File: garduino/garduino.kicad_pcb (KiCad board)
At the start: 2 copper layers, 65 x 56 mm, 54 parts, among them J1 ADC1, J10 OUT6, J11 ADC7, J12 OUT5, J13 OUT4, J14 DIN, J15 OUT3, J16 12v, J17 OUT2, J18 OUT1, J19 RPi, J2 ADC2, J3 ADC3, J4 Max7219, J5 ADC4, J6 ADC5, J7 OUT8, J8 OUT7, J9 ADC6, Q1 NCV8403, Q10 BSS138, Q11 BSS138, Q12 NCV8403, Q2 NCV8403, Q3 NCV8403, Q4 NCV8403, Q5 NCV8403, Q6 NCV8403, Q7 NCV8403, Q8 BSS138, Q9 BSS138, SW1 SW_DIP_x01, U2 ATmega328P-AU, Y1 Crystal

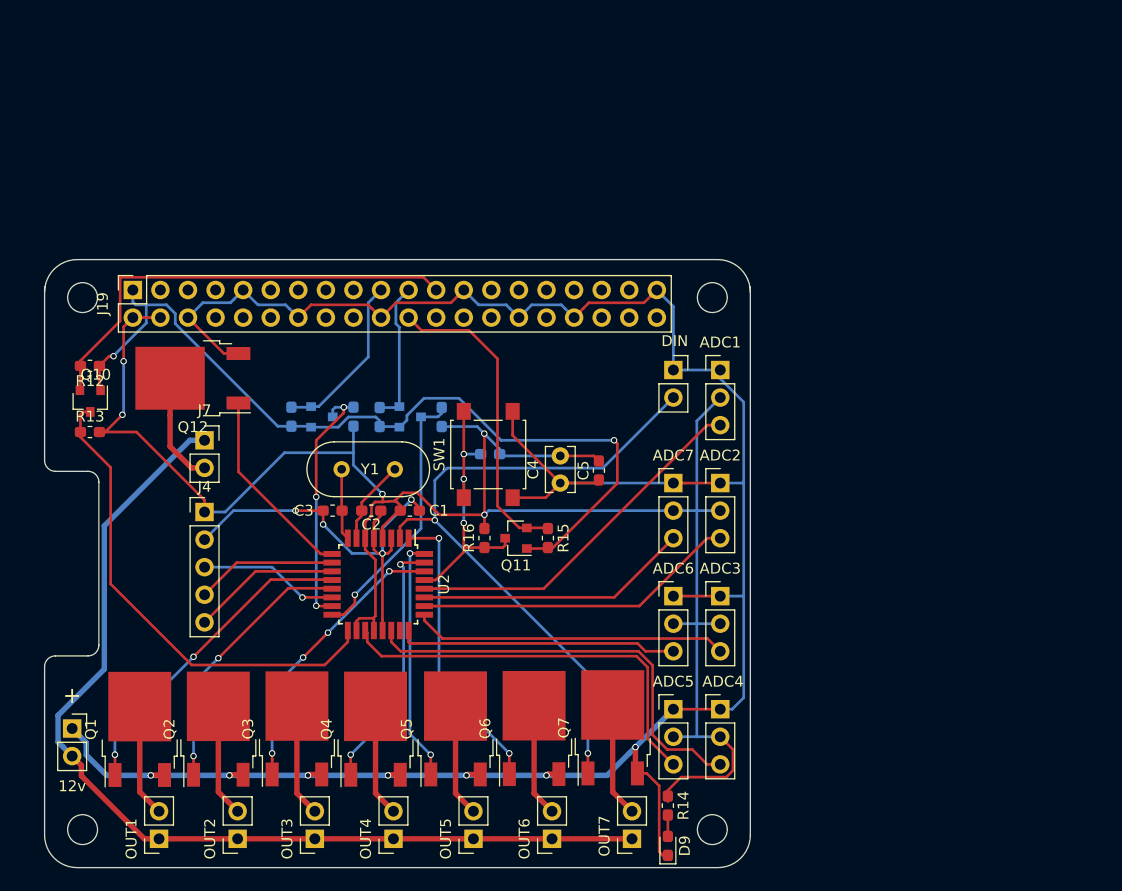
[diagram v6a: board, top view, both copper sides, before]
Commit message: Guarduino switched to MCP3008, PCB not done
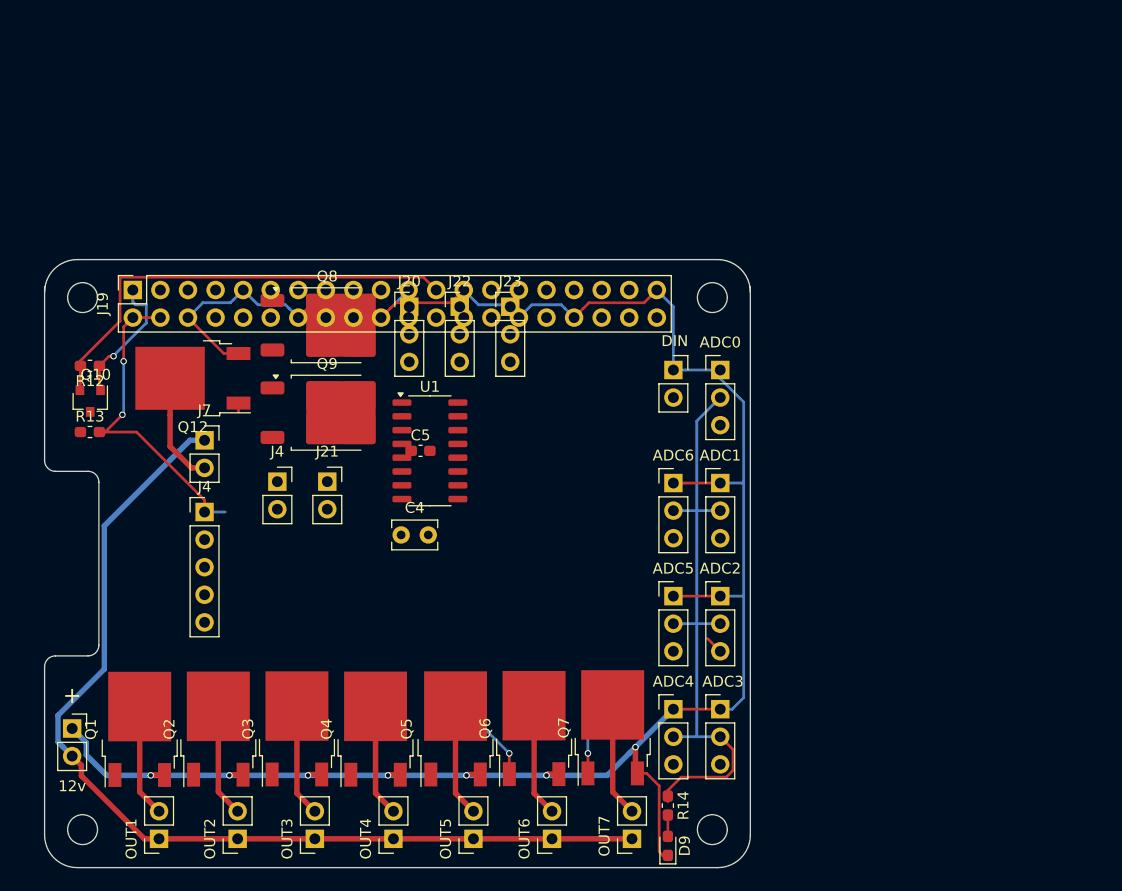
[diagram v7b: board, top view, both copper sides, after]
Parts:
- removed C1: 100n, Capacitor_SMD:C_0603_1608Metric_Pad1.05x0.95mm_HandSolder
- removed C2, C3: 22pF, Capacitor_SMD:C_0603_1608Metric_Pad1.05x0.95mm_HandSolder
- removed Q11: BSS138, Package_TO_SOT_SMD:SOT-23
- removed R10, R11, R15, R16, R17, R8, R9: 10k, Resistor_SMD:R_0603_1608Metric_Pad1.05x0.95mm_HandSolder
- removed SW1: SW_DIP_x01, Button_Switch_SMD:SW_SPST_B3S-1000
- removed U2: ATmega328P-AU, Package_QFP:TQFP-32_7x7mm_P0.8mm
- removed Y1: Crystal, Crystal:Crystal_HC18-U_Vertical
- added J20: ADC7, Connector_PinHeader_2.54mm:PinHeader_1x03_P2.54mm_Vertical, F.Cu at (123.2, 93.0)
- added J21: OUT1, Connector_PinSocket_2.54mm:PinSocket_1x02_P2.54mm_Vertical, F.Cu at (115.7, 109.1)
- added J22: ADC8, Connector_PinHeader_2.54mm:PinHeader_1x03_P2.54mm_Vertical, F.Cu at (127.9, 93.0)
- added J23: ADC9, Connector_PinHeader_2.54mm:PinHeader_1x03_P2.54mm_Vertical, F.Cu at (132.6, 93.0)
- added J4: OUT1, Connector_PinSocket_2.54mm:PinSocket_1x02_P2.54mm_Vertical, F.Cu at (111.1, 109.1)
- added U1: MCP3008, Package_SO:SO-16_3.9x9.9mm_P1.27mm, F.Cu at (125.2, 106.2)
- C5: footprint Capacitor_SMD:C_0603_1608Metric_Pad1.05x0.95mm_HandSolder -> Capacitor_SMD:C_0603_1608Metric_Pad1.08x0.95mm_HandSolder
- J1: value ADC1 -> ADC0
- J11: value ADC7 -> ADC6
- J2: value ADC2 -> ADC1
- J3: value ADC3 -> ADC2
- J5: value ADC4 -> ADC3
- J6: value ADC5 -> ADC4
- J9: value ADC6 -> ADC5
- Q8, Q9: value BSS138 -> NCV8403; footprint Package_TO_SOT_SMD:SOT-23 -> Package_TO_SOT_SMD:TO-252-2; moved to F.Cu
- moved C5 16.5 mm to (124.3, 106.2), turned to 0 degrees
- moved C4 15.4 mm to (122.5, 114.0), turned to 0 degrees
- moved Q8 8.45 mm to (115.7, 94.7)
- moved Q9 7.65 mm to (115.7, 102.7)
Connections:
- J1 pad 3: /PC5 -> /CH0
- J11 pad 3: /PC4 -> /CH6
- J19 pad 1: +3V3 -> +3.3V
- J19 pad 10: (no net) -> /RXD
- J19 pad 11: (no net) -> /SPI1_CE1
- J19 pad 12: (no net) -> /SPI1_CE0
- J19 pad 13: (no net) -> /GPIO27
- J19 pad 15: (no net) -> /GPIO22
- J19 pad 16: (no net) -> /GPIO23
- J19 pad 17: (no net) -> +3.3V
- J19 pad 18: (no net) -> /GPIO24
- J19 pad 22: /BCM25 -> /GPIO25
- J19 pad 24: (no net) -> /SPI0_CE0
- J19 pad 26: (no net) -> /SPI0_CE1
- J19 pad 27: (no net) -> /GPIO0
- J19 pad 28: (no net) -> /GPIO1
- J19 pad 29: (no net) -> /GPIO5
- J19 pad 3: (no net) -> /SDA
- J19 pad 31: (no net) -> /GPIO6
- J19 pad 32: (no net) -> /PWM0
- J19 pad 33: (no net) -> /PWM1
- J19 pad 35: (no net) -> /SPI1_MISO
- J19 pad 36: (no net) -> /SPI1_CE2
- J19 pad 37: (no net) -> /GPIO26
- J19 pad 38: (no net) -> /SPI1_MOSI
- J19 pad 40: (no net) -> /SPI1_SCLK
- J19 pad 5: (no net) -> /SCL
- J19 pad 7: (no net) -> /GPIO4
- J19 pad 8: (no net) -> /TXD
- J2 pad 3: /PC3 -> /CH1
- J3 pad 3: /PC2 -> /CH2
- J5 pad 3: /ADC7 -> /CH3
- J6 pad 3: /ADC6 -> /CH4
- J9 pad 3: /PC1 -> /CH5
- Q1 pad 1: /PB0 -> /GPIO4
- Q10 pad 1: +3V3 -> +3.3V
- Q12 pad 1: /PD5 -> /GPIO24
- Q2 pad 1: /PB1 -> /GPIO27
- Q3 pad 1: /PD0 -> /GPIO22
- Q4 pad 1: /PD1 -> /GPIO0
- Q5 pad 1: /PD2 -> /GPIO5
- Q6 pad 1: /PD3 -> /GPIO6
- Q7 pad 1: /PD4 -> /GPIO23
- Q8 pad 1: +3V3 -> /GPIO25
- Q8 pad 2: /SPI0_MOSI -> /OUT8
- Q8 pad 3: /MOSI -> GND
- Q9 pad 1: +3V3 -> /GPIO1
- Q9 pad 2: /SPI0_MISO -> /OUT9
- Q9 pad 3: /MISO -> GND
- R12 pad 2: +3V3 -> +3.3V
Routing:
- net +5V: track 182.0 -> 86.6 mm, vias 5 -> 2
- net +3V3: track 79.7 -> 0.00 mm, vias 2 -> 0
- net GND: track 269.3 -> 200.7 mm, vias 11 -> 7
- net /PD4: track 62.5 -> 0.00 mm, vias 2 -> 0
- net /SCLK: track 44.6 -> 0.00 mm
- net /ADC7: track 39.8 -> 0.00 mm
- net /ADC6: track 37.8 -> 0.00 mm
- net /PC5: track 33.5 -> 0.00 mm
- net /PC3: track 29.8 -> 0.00 mm
- net /PB0: track 29.6 -> 0.00 mm, vias 2 -> 0
- net /PC2: track 29.0 -> 0.00 mm
- net /BCM25: track 28.8 -> 0.00 mm
- net /PD3: track 27.2 -> 0.00 mm, vias 2 -> 0
- net /PD0: track 26.6 -> 0.00 mm, vias 4 -> 0
- net /PC1: track 25.8 -> 0.00 mm
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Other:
- net class Default removed

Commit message: Cleanups, placement might work
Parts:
- removed the J14 at (147.6, 98.8)
- removed the J4 at (104.4, 111.9)
- removed the Q10 at (93.9, 101.7)
- removed R12, R13: 10k, Resistor_SMD:R_0603_1608Metric_Pad1.05x0.95mm_HandSolder
- J10: renamed from J8; value OUT7 -> OUT6
- J11: renamed from J7; value OUT8 -> OUT7
- J12: renamed from J21; value OUT1 -> OUT8
- J13: renamed from J4; value OUT1 -> OUT9
- J4: renamed from J18; value OUT1 -> OUT0
- J5: renamed from J17; value OUT2 -> OUT1
- J6: renamed from J15; value OUT3 -> OUT2
- J7: renamed from J13; value OUT4 -> OUT3
- J8: renamed from J12; value OUT5 -> OUT4
- J9: renamed from J10; value OUT6 -> OUT5
- moved R1 56.3 mm to (96.0, 115.2)
- moved D1 56.3 mm to (96.0, 118.9)
- moved J11 47.5 mm to (134.5, 142.0), turned to 180 degrees
- moved J13 46.9 mm to (144.5, 142.0), turned to 180 degrees
- moved J23 46.1 mm to (151.5, 135.0), turned to -90 degrees
- moved J22 44.4 mm to (151.6, 130.5), turned to -90 degrees
- moved J21 43.5 mm to (151.5, 126.0), turned to -90 degrees
- moved J12 40.6 mm to (139.5, 142.0), turned to 180 degrees
- moved Q4 31.3 mm to (113.0, 120.0)
- moved Q8 27.4 mm to (128.0, 119.2), turned to 90 degrees
- moved Q5 26.7 mm to (120.5, 120.0), turned to 90 degrees
- moved Q10 26.0 mm to (135.8, 119.2), turned to 90 degrees
- moved J17 20.1 mm to (151.5, 110.0), turned to -90 degrees
- moved J18 16.5 mm to (151.5, 114.0), turned to -90 degrees
- moved J10 14.3 mm to (129.5, 142.0)
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- renumbered C4 to C1, C5 to C2, D9 to D1, J19 to J1, J1 to J14, J2 to J15, J3 to J16, J5 to J17, J6 to J18, J9 to J19, J11 to J20, J20 to J21, J16 to J3, Q9 to Q10, Q6 to Q2, Q2 to Q3, Q7 to Q4, Q12 to Q5, Q3 to Q6, Q4 to Q7, Q5 to Q9, R14 to R1
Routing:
- net +12V: track 91.3 -> 11.7 mm
- net +5V: track 86.6 -> 24.1 mm, vias 2 -> 0
- net /GPIO4: track 0.00 -> 50.5 mm
- net /SPI0_SCLK: track 41.5 -> 1.75 mm
- net GND: track 200.7 -> 179.0 mm, vias 7 -> 6
- net +3.3V: track 12.4 -> 0.00 mm, vias 1 -> 0
- net /GPIO6: track 11.1 -> 0.00 mm, vias 1 -> 0
- net /OUT6: track 10.5 -> 0.00 mm
- net /OUT5: track 10.4 -> 0.00 mm
- net /OUT2: track 10.4 -> 0.00 mm
- net /OUT7: track 10.3 -> 0.00 mm
- net /GPIO23: track 9.21 -> 0.00 mm, vias 1 -> 0
- net /OUT1: track 10.4 -> 7.88 mm
- net /OUT3: track 10.3 -> 8.01 mm
- net /OUT4: track 10.4 -> 8.03 mm
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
